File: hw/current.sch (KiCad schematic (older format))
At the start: 22 parts, among them J301 Conn_01x02, J302 Conn_01x02, U301 LP2985-5.0, U302 ACS770xCB-100U-PSF, U303 MCP6001-OT, U304 ACS770xCB-100U-PSF, U305 MCP6001-OT

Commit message: Pin remapping and layout improvements
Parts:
- C301: footprint Capacitors_SMD:C_0603 -> Capacitor_SMD:C_0603_1608Metric_Pad1.05x0.95mm_HandSolder
- C302, C303, C304, C306, C307: footprint Capacitors_SMD:C_0603_HandSoldering -> Capacitor_SMD:C_0603_1608Metric_Pad1.05x0.95mm_HandSolder
- C309: footprint Capacitors_SMD:C_0805 -> Capacitor_SMD:C_0805_2012Metric_Pad1.15x1.40mm_HandSolder
- R301, R302, R303, R304, R305, R306, R307, R308: footprint Resistors_SMD:R_0603_HandSoldering -> Resistor_SMD:R_0603_1608Metric_Pad1.05x0.95mm_HandSolder
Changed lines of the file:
@@
 F 0 "R301" H 6709 3046 50  0000 L CNN
 F 1 "68k" H 6709 2955 50  0000 L CNN
-F 2 "Resistors_SMD:R_0603_HandSoldering" H 6650 3000 50  0001 C CNN
+F 2 "Resistor_SMD:R_0603_1608Metric_Pad1.05x0.95mm_HandSolder" H 6650 3000 50  0001 C CNN
 F 3 "~" H 6650 3000 50  0001 C CNN
 	1    6650 3000
@@
 F 0 "R302" H 6709 3346 50  0000 L CNN
 F 1 "12k" H 6709 3255 50  0000 L CNN
-F 2 "Resistors_SMD:R_0603_HandSoldering" H 6650 3300 50  0001 C CNN
+F 2 "Resistor_SMD:R_0603_1608Metric_Pad1.05x0.95mm_HandSolder" H 6650 3300 50  0001 C CNN
 F 3 "~" H 6650 3300 50  0001 C CNN
 	1    6650 3300
@@
 F 0 "R303" H 6709 5346 50  0000 L CNN
 F 1 "68k" H 6709 5255 50  0000 L CNN
-F 2 "Resistors_SMD:R_0603_HandSoldering" H 6650 5300 50  0001 C CNN
+F 2 "Resistor_SMD:R_0603_1608Metric_Pad1.05x0.95mm_HandSolder" H 6650 5300 50  0001 C CNN
 F 3 "~" H 6650 5300 50  0001 C CNN
 	1    6650 5300
@@
 F 0 "R304" H 6709 5646 50  0000 L CNN
 F 1 "12k" H 6709 5555 50  0000 L CNN
-F 2 "Resistors_SMD:R_0603_HandSoldering" H 6650 5600 50  0001 C CNN
+F 2 "Resistor_SMD:R_0603_1608Metric_Pad1.05x0.95mm_HandSolder" H 6650 5600 50  0001 C CNN
 F 3 "~" H 6650 5600 50  0001 C CNN
 	1    6650 5600
@@
 F 0 "C303" V 6771 1750 50  0000 C CNN
 F 1 "100n" V 6862 1750 50  0000 C CNN
-F 2 "Capacitors_SMD:C_0603_HandSoldering" H 7000 1750 50  0001 C CNN
+F 2 "Capacitor_SMD:C_0603_1608Metric_Pad1.05x0.95mm_HandSolder" H 7000 1750 50  0001 C CNN
 F 3 "~" H 7000 1750 50  0001 C CNN
 	1    7000 1750
@@
 F 0 "C306" V 6621 4000 50  0000 C CNN
 F 1 "100n" V 6712 4000 50  0000 C CNN
-F 2 "Capacitors_SMD:C_0603_HandSoldering" H 6850 4000 50  0001 C CNN
+F 2 "Capacitor_SMD:C_0603_1608Metric_Pad1.05x0.95mm_HandSolder" H 6850 4000 50  0001 C CNN
 F 3 "~" H 6850 4000 50  0001 C CNN
 	1    6850 4000
@@
 F 0 "C307" V 7771 5200 50  0000 C CNN
 F 1 "100n" V 7862 5200 50  0000 C CNN
-F 2 "Capacitors_SMD:C_0603_HandSoldering" H 8000 5200 50  0001 C CNN
+F 2 "Capacitor_SMD:C_0603_1608Metric_Pad1.05x0.95mm_HandSolder" H 8000 5200 50  0001 C CNN
 F 3 "~" H 8000 5200 50  0001 C CNN
 	1    8000 5200
@@
 F 0 "C304" V 7821 2900 50  0000 C CNN
 F 1 "100n" V 7912 2900 50  0000 C CNN
-F 2 "Capacitors_SMD:C_0603_HandSoldering" H 8050 2900 50  0001 C CNN
+F 2 "Capacitor_SMD:C_0603_1608Metric_Pad1.05x0.95mm_HandSolder" H 8050 2900 50  0001 C CNN
 F 3 "~" H 8050 2900 50  0001 C CNN
 	1    8050 2900
@@
 F 0 "R305" V 7604 2100 50  0000 C CNN
 F 1 "12k" V 7700 2100 50  0000 C CNN
-F 2 "Resistors_SMD:R_0603_HandSoldering" H 7800 2100 50  0001 C CNN
+F 2 "Resistor_SMD:R_0603_1608Metric_Pad1.05x0.95mm_HandSolder" H 7800 2100 50  0001 C CNN
 F 3 "~" H 7800 2100 50  0001 C CNN
 	1    7800 2100
@@
 F 0 "R306" H 8009 2296 50  0000 L CNN
 F 1 "18k" H 8009 2205 50  0000 L CNN
-F 2 "Resistors_SMD:R_0603_HandSoldering" H 7950 2250 50  0001 C CNN
+F 2 "Resistor_SMD:R_0603_1608Metric_Pad1.05x0.95mm_HandSolder" H 7950 2250 50  0001 C CNN
 F 3 "~" H 7950 2250 50  0001 C CNN
 	1    7950 2250
@@
 F 0 "R307" V 7604 4350 50  0000 C CNN
 F 1 "12k" V 7700 4350 50  0000 C CNN
-F 2 "Resistors_SMD:R_0603_HandSoldering" H 7800 4350 50  0001 C CNN
+F 2 "Resistor_SMD:R_0603_1608Metric_Pad1.05x0.95mm_HandSolder" H 7800 4350 50  0001 C CNN
 F 3 "~" H 7800 4350 50  0001 C CNN
 	1    7800 4350
@@
 F 0 "R308" H 8009 4546 50  0000 L CNN
 F 1 "18k" H 8009 4455 50  0000 L CNN
-F 2 "Resistors_SMD:R_0603_HandSoldering" H 7950 4500 50  0001 C CNN
+F 2 "Resistor_SMD:R_0603_1608Metric_Pad1.05x0.95mm_HandSolder" H 7950 4500 50  0001 C CNN
 F 3 "~" H 7950 4500 50  0001 C CNN
 	1    7950 4500
@@
 F 0 "C302" H 4342 1396 50  0000 L CNN
 F 1 "10n" H 4342 1305 50  0000 L CNN
-F 2 "Capacitors_SMD:C_0603_HandSoldering" H 4250 1350 50  0001 C CNN
+F 2 "Capacitor_SMD:C_0603_1608Metric_Pad1.05x0.95mm_HandSolder" H 4250 1350 50  0001 C CNN
 F 3 "~" H 4250 1350 50  0001 C CNN
 	1    4250 1350
@@
 F 0 "C301" H 2858 1304 50  0000 R CNN
 F 1 "1u" H 2858 1395 50  0000 R CNN
-F 2 "Capacitors_SMD:C_0603" H 2950 1350 50  0001 C CNN
+F 2 "Capacitor_SMD:C_0603_1608Metric_Pad1.05x0.95mm_HandSolder" H 2950 1350 50  0001 C CNN
 F 3 "~" H 2950 1350 50  0001 C CNN
 	1    2950 1350
@@
 F 0 "C309" H 4508 1304 50  0000 R CNN
 F 1 "2u2" H 4508 1395 50  0000 R CNN
-F 2 "Capacitors_SMD:C_0805" H 4600 1350 50  0001 C CNN
+F 2 "Capacitor_SMD:C_0805_2012Metric_Pad1.15x1.40mm_HandSolder" H 4600 1350 50  0001 C CNN
 F 3 "~" H 4600 1350 50  0001 C CNN
 	1    4600 1350

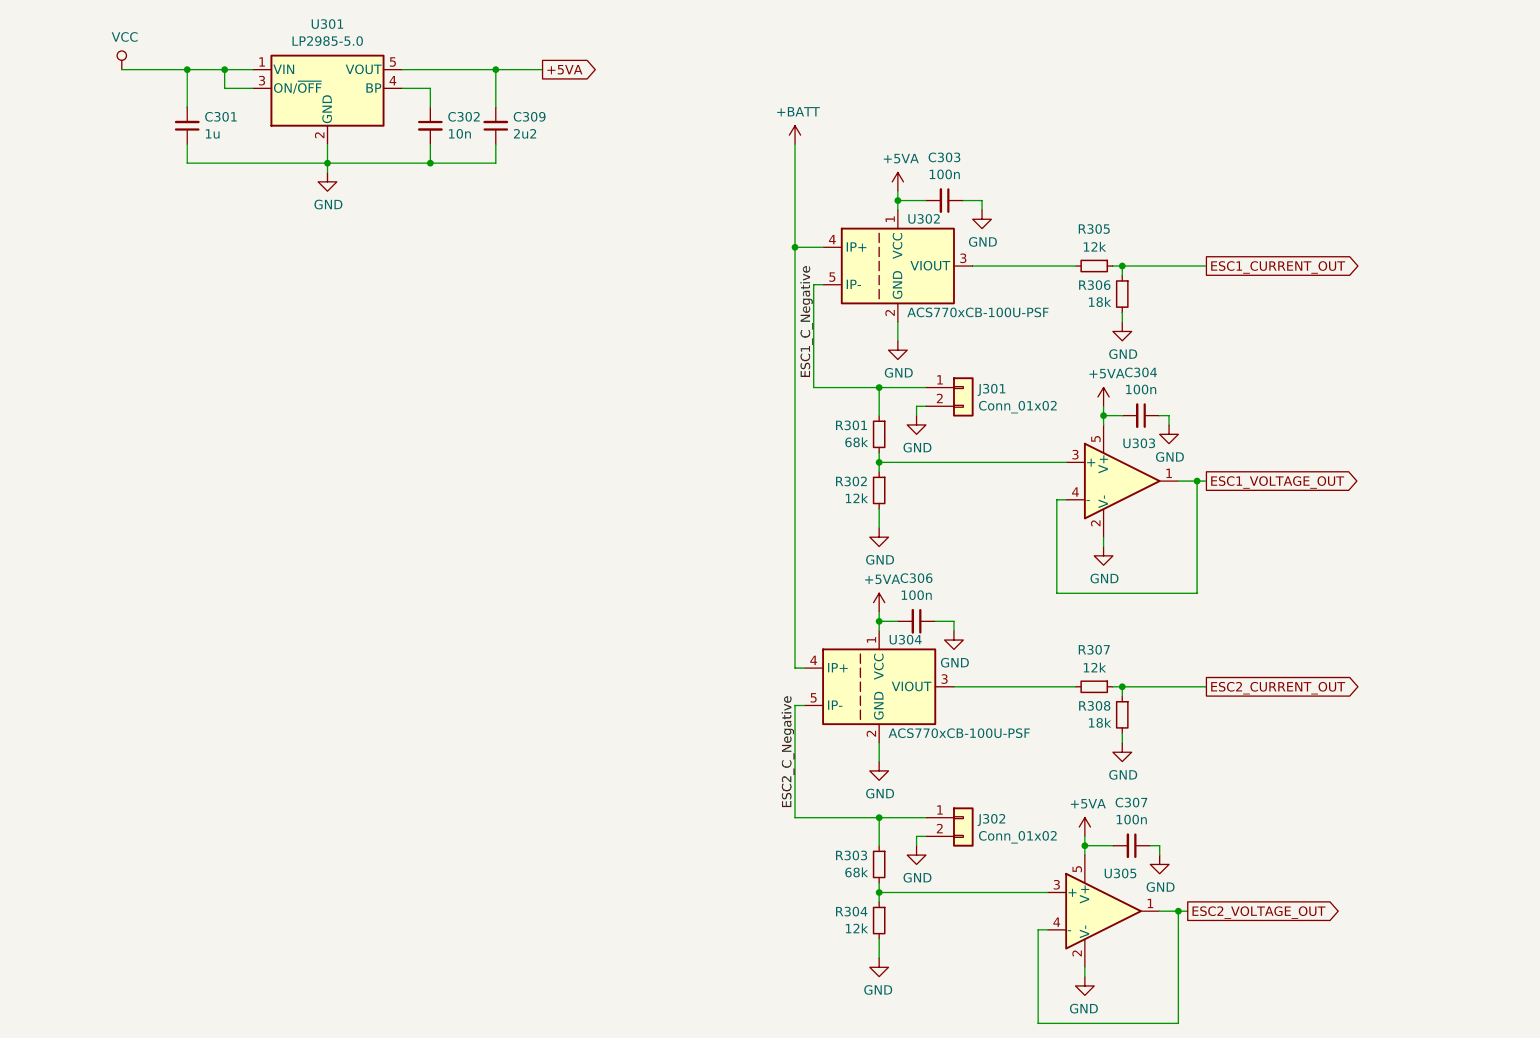
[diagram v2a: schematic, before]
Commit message: BOM Generation for 1.1 version
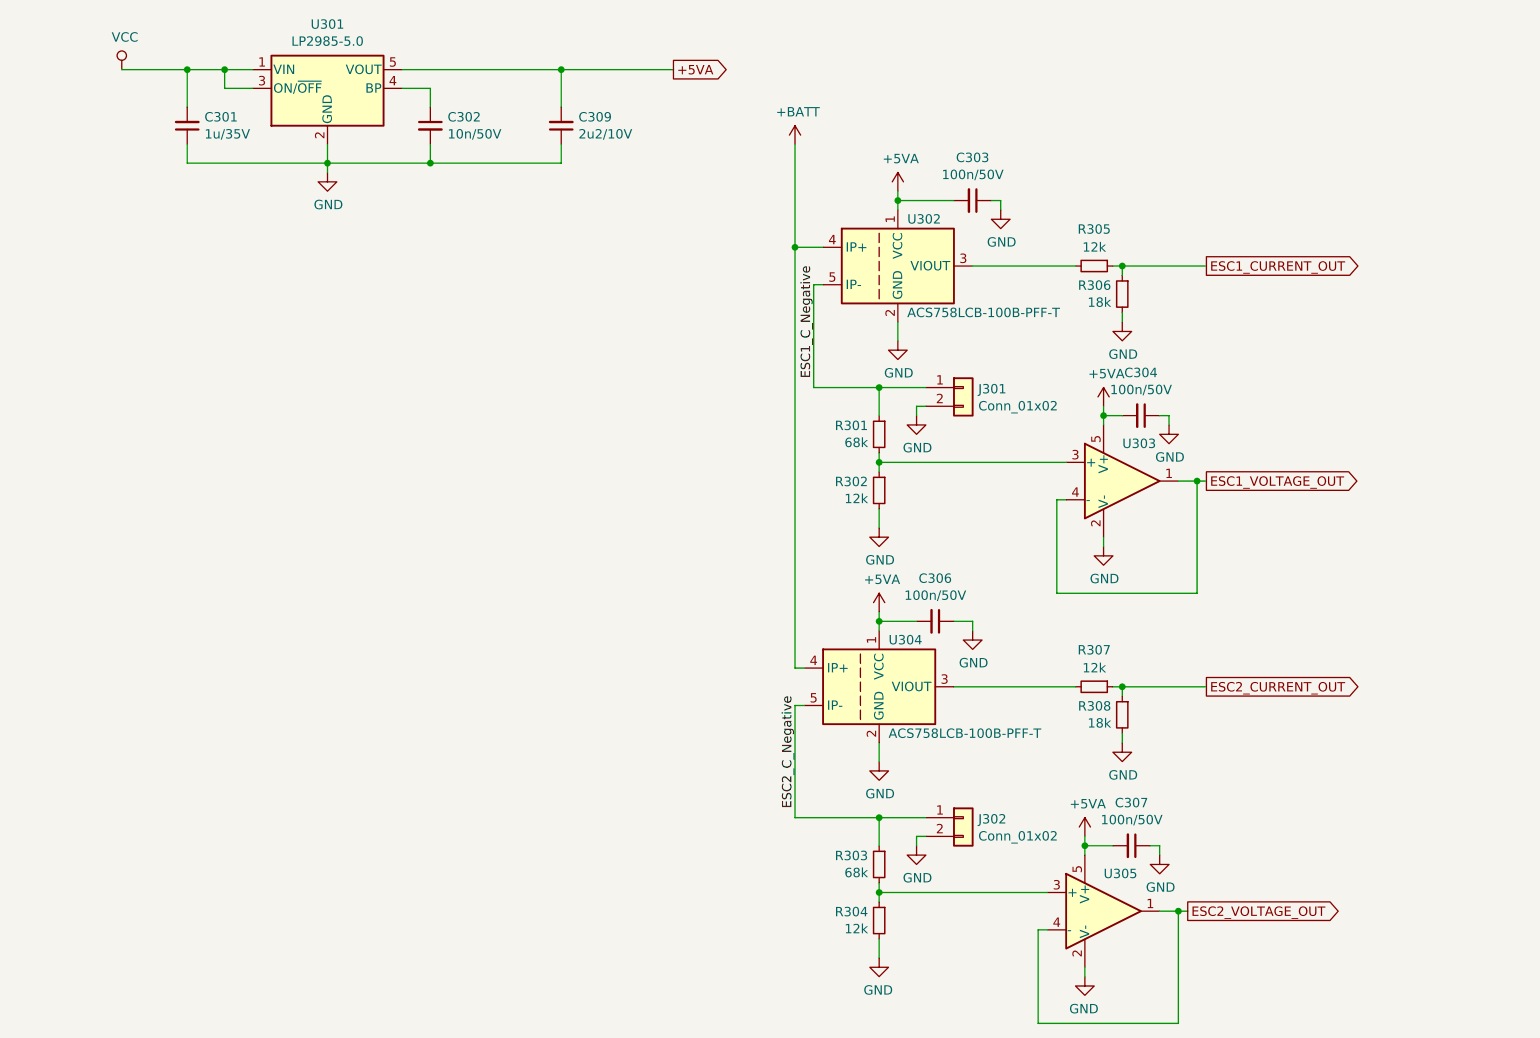
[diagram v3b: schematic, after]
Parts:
- C301: value 1u -> 1u/35V
- C302: value 10n -> 10n/50V
- C303, C304, C306, C307: value 100n -> 100n/50V
- C309: value 2u2 -> 2u2/10V
- J301, J302: Config (none) -> -prod
- U301: Description (none) -> Micropower 150-mA Low-Noise Ultra-Low-Dropout Regulator; MPN (none) -> LP2985-5.0; Manufacturer (none) -> Texas Instruments
- U302, U304: value ACS770xCB-100U-PSF -> ACS758LCB-100B-PFF-T; Config (none) -> -prod; Description (none) -> Thermally Enhanced, Fully Integrated, Hall-Effect-Based Lin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; MPN (none) -> ACS758LCB-100B-PFF-T; Manufacturer (none) -> Allegro
- U303, U305: MPN (none) -> MCP6001-OT; Manufacturer (none) -> Microchip
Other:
- moved on the sheet: C303, C306, C309
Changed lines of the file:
@@
 Sheet 3 4
 Title "RC Telemetry board"
-Date "2020-02-12"
-Rev "0.2"
+Date "2020-02-23"
+Rev "1.1"
 Comp "www.findersee.fi"
 Comment1 "https://github.com/findersee/rctelemetry"
@@
 P 6750 2100
 F 0 "U302" H 6800 2350 50  0000 L CNN
-F 1 "ACS770xCB-100U-PSF" H 6800 1850 50  0000 L CNN
+F 1 "ACS758LCB-100B-PFF-T" H 6800 1850 50  0000 L CNN
 F 2 "PCBDecals:Allegro_PFF" H 6750 2100 50  0001 C CNN
 F 3 "http://www.allegromicro.com/~/media/Files/Datasheets/ACS758-Datasheet.ashx?la=en" H 6750 2100 50  0001 C CNN
+F 4 "-prod" H 6750 2100 50  0001 C CNN "Config"
+F 5 "ACS758LCB-100B-PFF-T" H 6750 2100 50  0001 C CNN "MPN"
+F 6 "Allegro" H 6750 2100 50  0001 C CNN "Manufacturer"
+F 7 "Thermally Enhanced, Fully Integrated, Hall-Effect-Based Linear Current Sensor IC with 100 µΩ Current Conductor" H 6750 2100 50  0001 C CNN "Description"
 	1    6750 2100
-	1    0    0    -1
-$EndComp
-$Comp
-L Sensor_Current:ACS770xCB-100U-PSF U304
-U 1 1 5CE3A9FD
-P 6650 4350
-F 0 "U304" H 6700 4600 50  0000 L CNN
-F 1 "ACS770xCB-100U-PSF" H 6700 4100 50  0000 L CNN
-F 2 "PCBDecals:Allegro_PFF" H 6650 4350 50  0001 C CNN
-F 3 "http://www.allegromicro.com/~/media/Files/Datasheets/ACS758-Datasheet.ashx?la=en" H 6650 4350 50  0001 C CNN
-	1    6650 4350
 	1    0    0    -1
 $EndComp
@@
 F 2 "PCBDecals:2Pin_4mm" H 7100 2750 50  0001 C CNN
 F 3 "~" H 7100 2750 50  0001 C CNN
+F 4 "-prod" H 7100 2750 50  0001 C CNN "Config"
 	1    7100 2750
 	1    0    0    -1
@@
 F 2 "PCBDecals:2Pin_4mm" H 7100 5050 50  0001 C CNN
 F 3 "~" H 7100 5050 50  0001 C CNN
+F 4 "-prod" H 7100 5050 50  0001 C CNN "Config"
 	1    7100 5050
 	1    0    0    -1
@@
 L Device:C_Small C303
 U 1 1 5CE5A73F
-P 7000 1750
-F 0 "C303" V 6771 1750 50  0000 C CNN
-F 1 "100n" V 6862 1750 50  0000 C CNN
-F 2 "Capacitor_SMD:C_0603_1608Metric_Pad1.05x0.95mm_HandSolder" H 7000 1750 50  0001 C CNN
-F 3 "~" H 7000 1750 50  0001 C CNN
-	1    7000 1750
+P 7150 1750
+F 0 "C303" V 6921 1750 50  0000 C CNN
+F 1 "100n/50V" V 7012 1750 50  0000 C CNN
+F 2 "Capacitor_SMD:C_0603_1608Metric_Pad1.05x0.95mm_HandSolder" H 7150 1750 50  0001 C CNN
+F 3 "~" H 7150 1750 50  0001 C CNN
+	1    7150 1750
 	0    1    1    0
-$EndComp
-$Comp
-L Device:C_Small C306
-U 1 1 5CE5A7C1
-P 6850 4000
-F 0 "C306" V 6621 4000 50  0000 C CNN
-F 1 "100n" V 6712 4000 50  0000 C CNN
-F 2 "Capacitor_SMD:C_0603_1608Metric_Pad1.05x0.95mm_HandSolder" H 6850 4000 50  0001 C CNN
-F 3 "~" H 6850 4000 50  0001 C CNN
-	1    6850 4000
-	0    1    1    0
-$EndComp
-$Comp
-L power:GND #PWR0313
-U 1 1 5CE5A8D9
-P 7050 4050
-F 0 "#PWR0313" H 7050 3800 50  0001 C CNN
-F 1 "GND" H 7055 3877 50  0000 C CNN
-F 2 "" H 7050 4050 50  0001 C CNN
-F 3 "" H 7050 4050 50  0001 C CNN
-	1    7050 4050
-	1    0    0    -1
 $EndComp
 $Comp
 L power:GND #PWR0305
 U 1 1 5CE5A980
-P 7200 1800
-F 0 "#PWR0305" H 7200 1550 50  0001 C CNN
-F 1 "GND" H 7205 1627 50  0000 C CNN
-F 2 "" H 7200 1800 50  0001 C CNN
-F 3 "" H 7200 1800 50  0001 C CNN
-	1    7200 1800
-	1    0    0    -1
-$EndComp
-Wire Wire Line
-	7100 1750 7200 1750
-Wire Wire Line
-	7200 1750 7200 1800
-Wire Wire Line
-	6900 1750 6750 1750
+P 7300 1800
+F 0 "#PWR0305" H 7300 1550 50  0001 C CNN
+F 1 "GND" H 7305 1627 50  0000 C CNN
+F 2 "" H 7300 1800 50  0001 C CNN
+F 3 "" H 7300 1800 50  0001 C CNN
+	1    7300 1800
+	1    0    0    -1
+$EndComp
+Wire Wire Line
+	7250 1750 7300 1750
+Wire Wire Line
+	7300 1750 7300 1800
+Wire Wire Line
+	7050 1750 6750 1750
 Connection ~ 6750 1750
 Wire Wire Line
 	6750 1750 6750 1800
 Wire Wire Line
-	6950 4000 7050 4000
-Wire Wire Line
-	7050 4000 7050 4050
-Wire Wire Line
-	6750 4000 6650 4000
+	6850 4000 6650 4000
 Connection ~ 6650 4000
 Wire Wire Line
@@
 P 8000 5200
 F 0 "C307" V 7771 5200 50  0000 C CNN
-F 1 "100n" V 7862 5200 50  0000 C CNN
+F 1 "100n/50V" V 7862 5200 50  0000 C CNN
 F 2 "Capacitor_SMD:C_0603_1608Metric_Pad1.05x0.95mm_HandSolder" H 8000 5200 50  0001 C CNN
 F 3 "~" H 8000 5200 50  0001 C CNN
@@
 P 8050 2900
 F 0 "C304" V 7821 2900 50  0000 C CNN
-F 1 "100n" V 7912 2900 50  0000 C CNN
+F 1 "100n/50V" V 7912 2900 50  0000 C CNN
 F 2 "Capacitor_SMD:C_0603_1608Metric_Pad1.05x0.95mm_HandSolder" H 8050 2900 50  0001 C CNN
 F 3 "~" H 8050 2900 50  0001 C CNN
@@
 Wire Wire Line
 	3700 1600 3700 1550
-Text GLabel 4850 1050 2    50   Output ~ 0
+Text GLabel 5550 1050 2    50   Output ~ 0
 +5VA
 Wire Wire Line
-	4850 1050 4600 1050
+	5550 1050 4950 1050
 $Comp
 L power:VCC #PWR0301
@@
 F 2 "TO_SOT_Packages_SMD:SOT-23-5_HandSoldering" H 3700 1475 50  0001 C CNN
 F 3 "http://www.ti.com/lit/ds/symlink/lp2985.pdf" H 3700 1150 50  0001 C CNN
+F 4 "Texas Instruments" H 3700 1150 50  0001 C CNN "Manufacturer"
+F 5 "LP2985-5.0" H 3700 1150 50  0001 C CNN "MPN"
+F 6 "Micropower 150-mA Low-Noise Ultra-Low-Dropout Regulator" H 3700 1150 50  0001 C CNN "Description"
 	1    3700 1150
 	1    0    0    -1
 $EndComp
 Wire Wire Line
-	4100 1050 4600 1050
-Connection ~ 4600 1050
+	4100 1050 4950 1050
+Connection ~ 4950 1050
 $Comp
 L Device:C_Small C302
@@
 P 4250 1350
 F 0 "C302" H 4342 1396 50  0000 L CNN
-F 1 "10n" H 4342 1305 50  0000 L CNN
+F 1 "10n/50V" H 4342 1305 50  0000 L CNN
 F 2 "Capacitor_SMD:C_0603_1608Metric_Pad1.05x0.95mm_HandSolder" H 4250 1350 50  0001 C CNN
 F 3 "~" H 4250 1350 50  0001 C CNN
@@
 Connection ~ 4250 1550
 Wire Wire Line
-	4250 1550 4600 1550
+	4250 1550 4950 1550
 Wire Wire Line
 	3300 1050 3150 1050
@@
 P 2950 1350
 F 0 "C301" H 2858 1304 50  0000 R CNN
-F 1 "1u" H 2858 1395 50  0000 R CNN
+F 1 "1u/35V" H 2858 1395 50  0000 R CNN
 F 2 "Capacitor_SMD:C_0603_1608Metric_Pad1.05x0.95mm_HandSolder" H 2950 1350 50  0001 C CNN
 F 3 "~" H 2950 1350 50  0001 C CNN
@@
 L Device:C_Small C309
 U 1 1 5CEC8EFA
-P 4600 1350
-F 0 "C309" H 4508 1304 50  0000 R CNN
-F 1 "2u2" H 4508 1395 50  0000 R CNN
-F 2 "Capacitor_SMD:C_0805_2012Metric_Pad1.15x1.40mm_HandSolder" H 4600 1350 50  0001 C CNN
-F 3 "~" H 4600 1350 50  0001 C CNN
-	1    4600 1350
+P 4950 1350
+F 0 "C309" H 4858 1304 50  0000 R CNN
+F 1 "2u2/10V" H 4858 1395 50  0000 R CNN
+F 2 "Capacitor_SMD:C_0805_2012Metric_Pad1.15x1.40mm_HandSolder" H 4950 1350 50  0001 C CNN
+F 3 "~" H 4950 1350 50  0001 C CNN
+	1    4950 1350
 	-1   0    0    1
 $EndComp
 Wire Wire Line
-	4600 1050 4600 1250
-Wire Wire Line
-	4600 1450 4600 1550
+	4950 1050 4950 1250
+Wire Wire Line
+	4950 1450 4950 1550
 Wire Wire Line
 	3700 1450 3700 1550
@@
 F 2 "TO_SOT_Packages_SMD:SOT-23-5_HandSoldering" H 7850 3050 50  0001 L CNN
 F 3 "http://ww1.microchip.com/downloads/en/DeviceDoc/21733j.pdf" H 7950 3450 50  0001 C CNN
+F 4 "Microchip" H 7950 3250 50  0001 C CNN "Manufacturer"
+F 5 "MCP6001-OT" H 7950 3250 50  0001 C CNN "MPN"
 	1    7950 3250
 	1    0    0    -1
@@
 F 2 "TO_SOT_Packages_SMD:SOT-23-5_HandSoldering" H 7750 5350 50  0001 L CNN
 F 3 "http://ww1.microchip.com/downloads/en/DeviceDoc/21733j.pdf" H 7850 5750 50  0001 C CNN
+F 4 "MCP6001-OT" H 7850 5550 50  0001 C CNN "MPN"
+F 5 "Microchip" H 7850 5550 50  0001 C CNN "Manufacturer"
 	1    7850 5550
 	1    0    0    -1
 $EndComp
+Wire Wire Line
+	7150 4000 7150 4050
+Wire Wire Line
+	7050 4000 7150 4000
+$Comp
+L power:GND #PWR0313
+U 1 1 5CE5A8D9
+P 7150 4050
+F 0 "#PWR0313" H 7150 3800 50  0001 C CNN
+F 1 "GND" H 7155 3877 50  0000 C CNN
+F 2 "" H 7150 4050 50  0001 C CNN
+F 3 "" H 7150 4050 50  0001 C CNN
+	1    7150 4050
+	1    0    0    -1
+$EndComp
+$Comp
+L Device:C_Small C306
+U 1 1 5CE5A7C1
+P 6950 4000
+F 0 "C306" V 6721 4000 50  0000 C CNN
+F 1 "100n/50V" V 6812 4000 50  0000 C CNN
+F 2 "Capacitor_SMD:C_0603_1608Metric_Pad1.05x0.95mm_HandSolder" H 6950 4000 50  0001 C CNN
+F 3 "~" H 6950 4000 50  0001 C CNN
+	1    6950 4000
+	0    1    1    0
+$EndComp
+$Comp
+L Sensor_Current:ACS770xCB-100U-PSF U304
+U 1 1 5CE3A9FD
+P 6650 4350
+F 0 "U304" H 6700 4600 50  0000 L CNN
+F 1 "ACS758LCB-100B-PFF-T" H 6700 4100 50  0000 L CNN
+F 2 "PCBDecals:Allegro_PFF" H 6650 4350 50  0001 C CNN
+F 3 "http://www.allegromicro.com/~/media/Files/Datasheets/ACS758-Datasheet.ashx?la=en" H 6650 4350 50  0001 C CNN
+F 4 "-prod" H 6650 4350 50  0001 C CNN "Config"
+F 5 "ACS758LCB-100B-PFF-T" H 6650 4350 50  0001 C CNN "MPN"
+F 6 "Allegro" H 6650 4350 50  0001 C CNN "Manufacturer"
+F 7 "Thermally Enhanced, Fully Integrated, Hall-Effect-Based Linear Current Sensor IC with 100 µΩ Current Conductor" H 6650 4350 50  0001 C CNN "Description"
+	1    6650 4350
+	1    0    0    -1
+$EndComp
